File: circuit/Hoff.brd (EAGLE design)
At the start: 59.1 x 59.1 mm, 25 parts, among them IC1 74595D(ROUND), IC2 24LC256SN

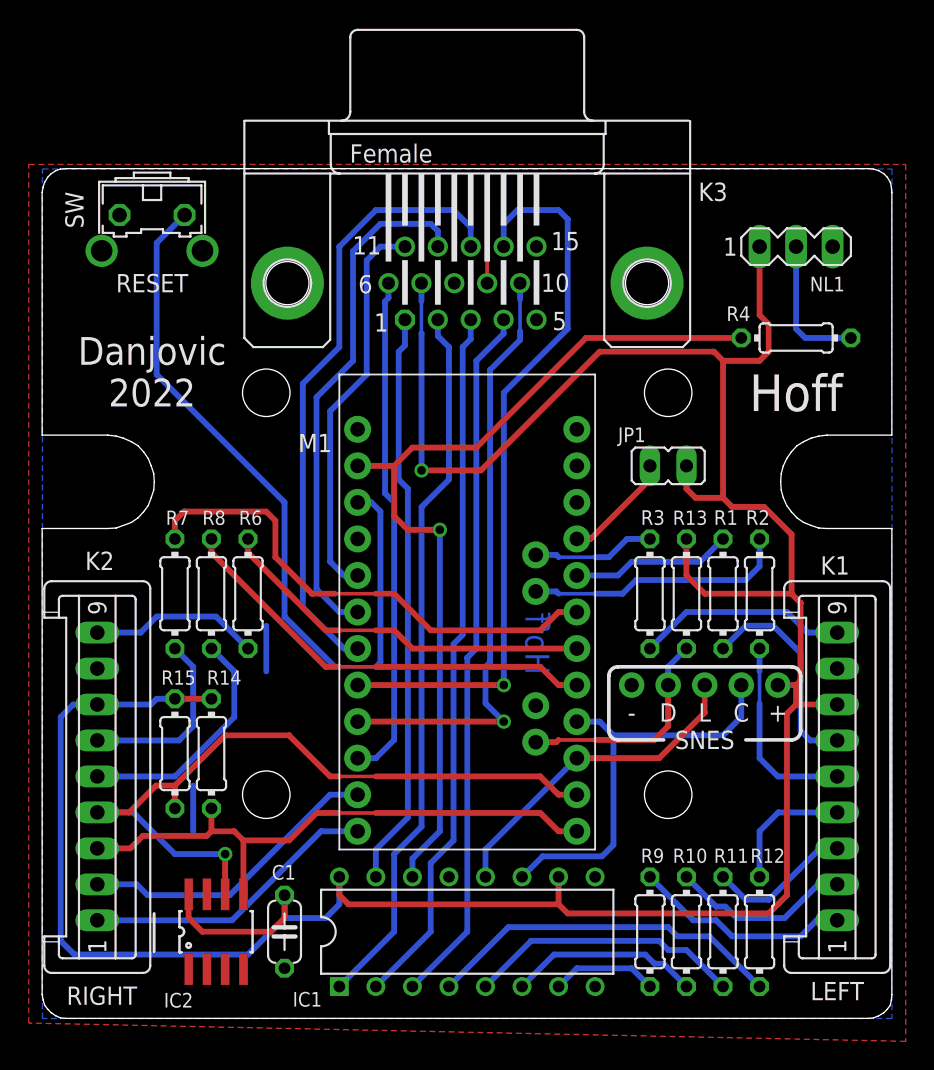
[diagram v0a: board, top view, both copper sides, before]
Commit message: Added neopixel to indicate operating mode
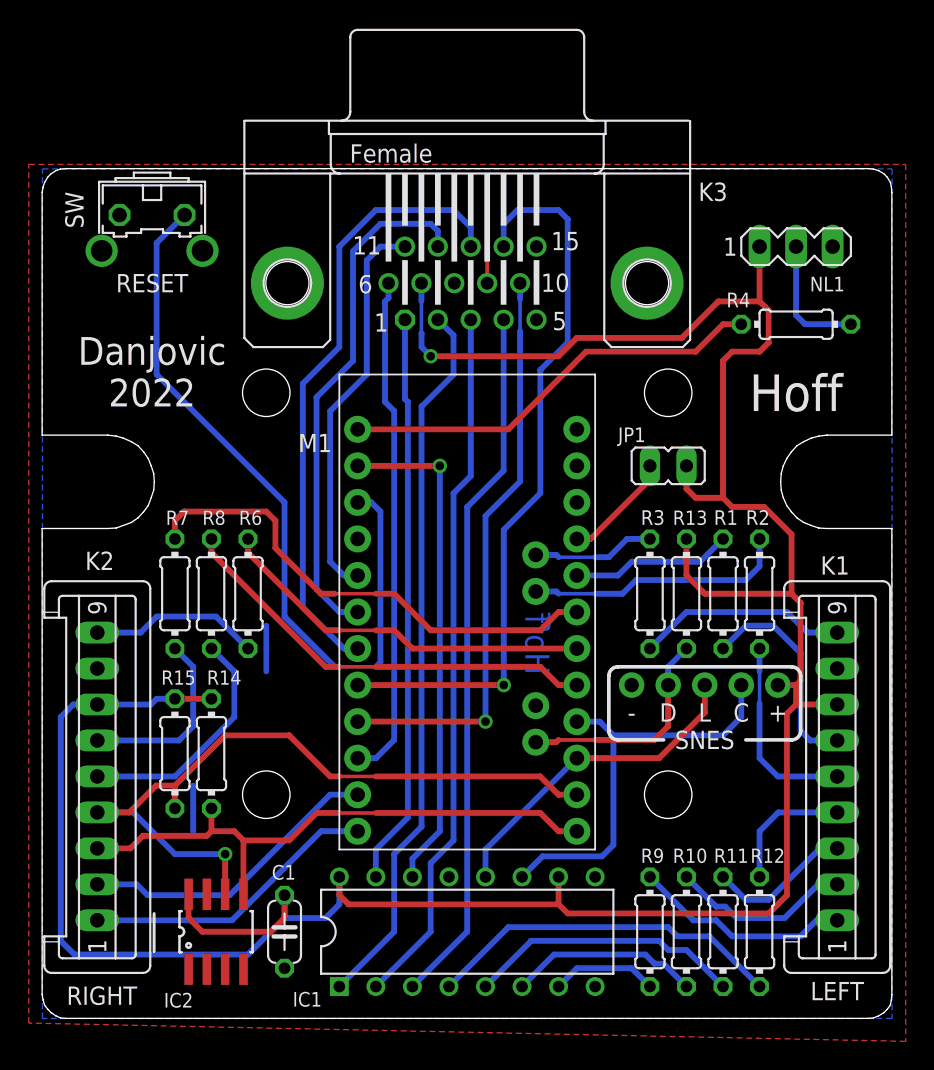
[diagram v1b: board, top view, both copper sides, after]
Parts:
- moved R4 0.95 mm to (53.3, 49.2)
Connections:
- new net LED: M1.TX0$1, R4.1
- net DATA: no longer R4.1
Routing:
- net LED: track 0.00 -> 29.7 mm
- net DATA: track 62.3 -> 35.1 mm
- net +5V: track 205.9 -> 197.7 mm
- net B1/B3: track 42.2 -> 40.4 mm
- net N$1: track 9.79 -> 8.84 mm
